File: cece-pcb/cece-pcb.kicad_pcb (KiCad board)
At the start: 2 copper layers, 57 x 80.5 mm, 52 parts, among them J1 SERIAL, J2 HTU21D, J3 Li-Ion Battery, J4 VAC, K1 SANYOU_SRD_Form_C, Q1 Q_NPN, Q2 Q_NPN, SW1 RES, U1 ESP-12F, U2 MCP73811T-420I-OT, U3 TLV75533PDBV

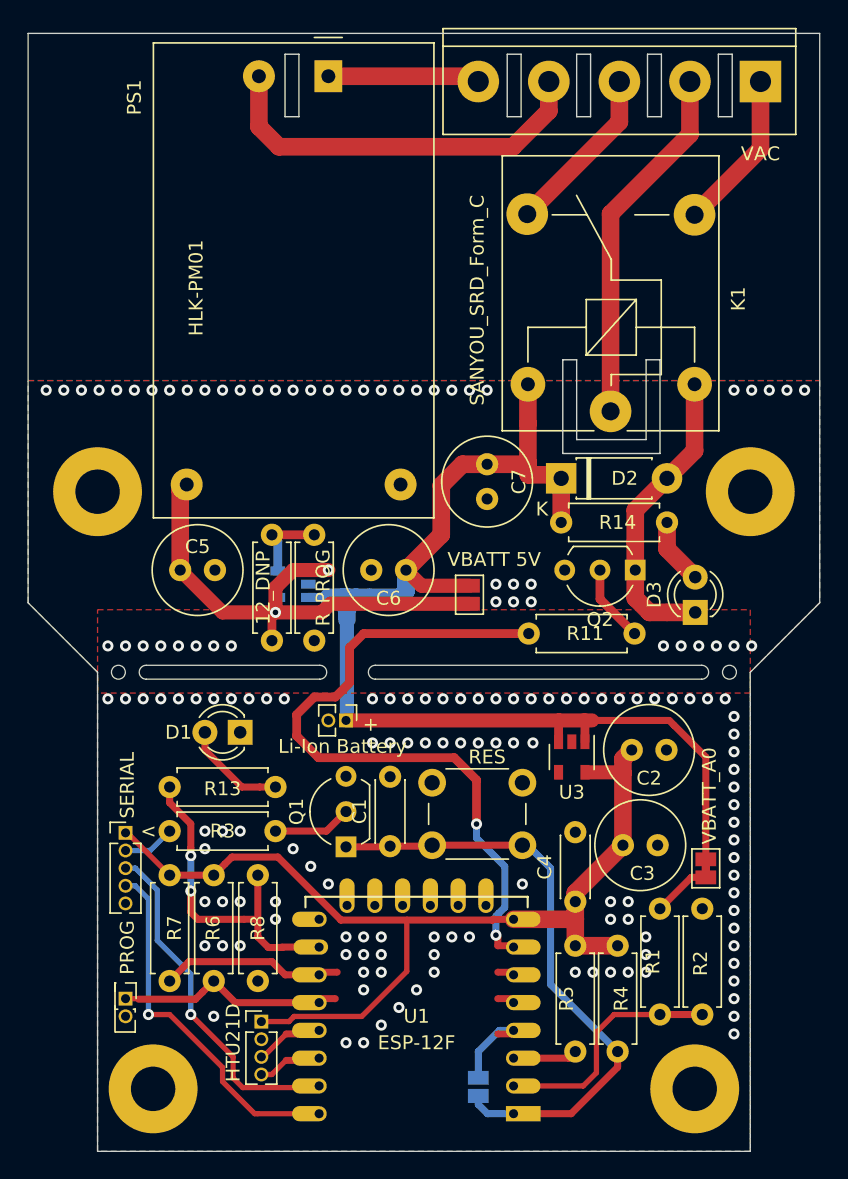
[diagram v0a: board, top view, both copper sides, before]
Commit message: Fix wrong footprint for the pin headers
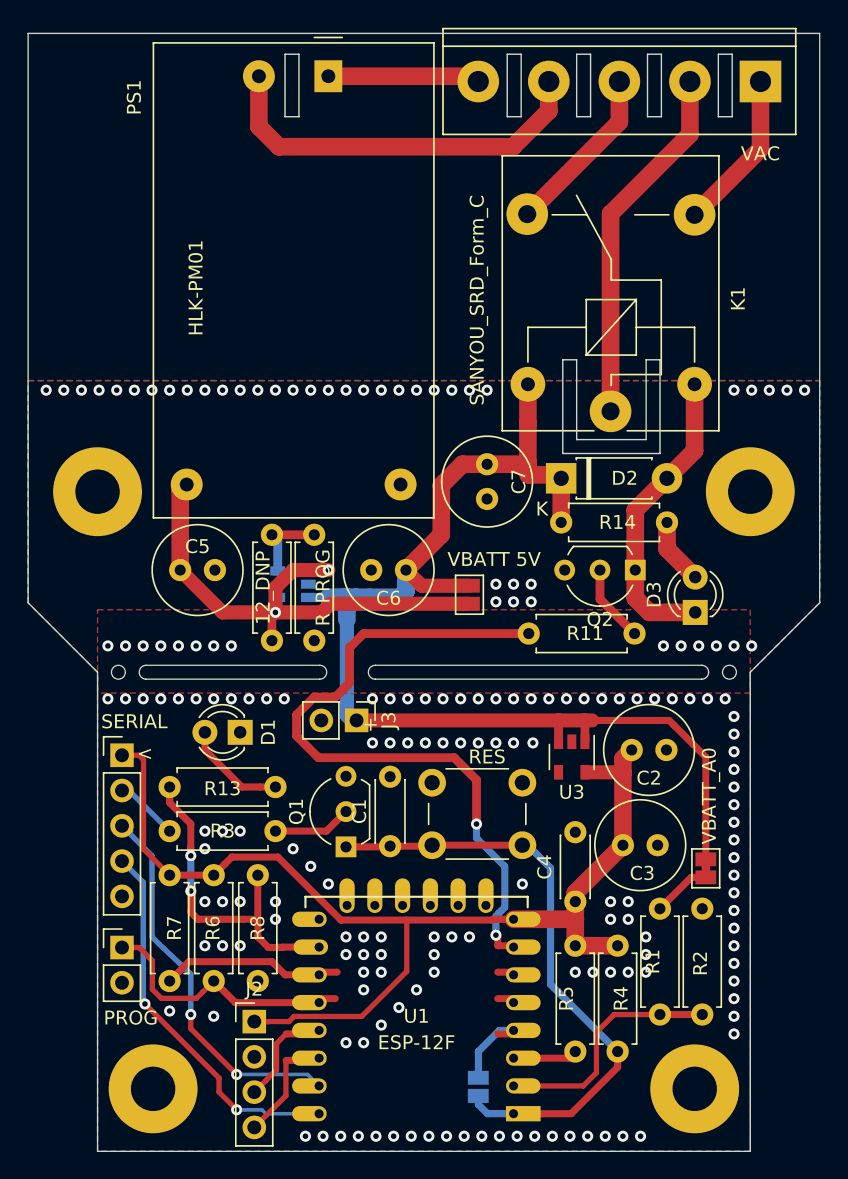
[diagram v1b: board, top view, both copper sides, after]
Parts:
- J1: footprint Connector_PinHeader_1.27mm:PinHeader_1x05_P1.27mm_Vertical -> Connector_PinHeader_2.54mm:PinHeader_1x05_P2.54mm_Vertical
- J2: footprint Connector_PinHeader_1.27mm:PinHeader_1x04_P1.27mm_Vertical -> Connector_PinHeader_2.54mm:PinHeader_1x04_P2.54mm_Vertical
- J3: footprint Connector_PinHeader_1.27mm:PinHeader_1x02_P1.27mm_Vertical -> Connector_PinHeader_2.54mm:PinHeader_1x02_P2.54mm_Vertical
- JP11: footprint Connector_PinHeader_1.27mm:PinHeader_2x01_P1.27mm_Vertical -> Connector_PinHeader_2.54mm:PinHeader_1x02_P2.54mm_Vertical
- moved J1 5.59 mm to (119.8, 86.0)
- moved JP11 3.69 mm to (119.8, 99.8), turned to 0 degrees
- moved J3 0.76 mm to (136.7, 83.5)
- moved J2 0.51 mm to (129.3, 105.2)
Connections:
- NT1 pad 1: (no net) -> /ESP-12_common/D0
- NT2 pad 1: (no net) -> /ESP-12_common/D5|SCK
- NT3 pad 1: (no net) -> /ESP-12_common/D6|MISO
- NT8 pad 2: (no net) -> /ESP-12_common/D3
- NT9 pad 2: (no net) -> /ESP-12_common/D4
- U1 pad 17: (no net) -> Net-(U1-Pad17)
- U1 pad 18: (no net) -> Net-(U1-Pad18)
- U1 pad 19: (no net) -> Net-(U1-Pad19)
- U1 pad 20: (no net) -> Net-(U1-Pad20)
- U1 pad 21: (no net) -> Net-(U1-Pad21)
- U1 pad 22: (no net) -> Net-(U1-Pad22)
- U3 pad 4: (no net) -> Net-(U3-Pad4)
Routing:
- net +3V3: track 73.3 -> 80.6 mm
- net /HTU_SCL: track 2.19 -> 5.77 mm
- net /RX: track 26.6 -> 29.8 mm, vias 1 -> 2
- net /ESP-12_common/GPIO0: track 16.7 -> 19.6 mm
- net /HTU_SDA: track 2.47 -> 5.14 mm
- net +BATT: track 89.4 -> 90.8 mm
- net /TX: track 26.2 -> 27.5 mm, vias 1 -> 2
- net /DTR: track 3.75 -> 4.64 mm
- net GND: track 0.00 -> 0.13 mm, vias 159 -> 180

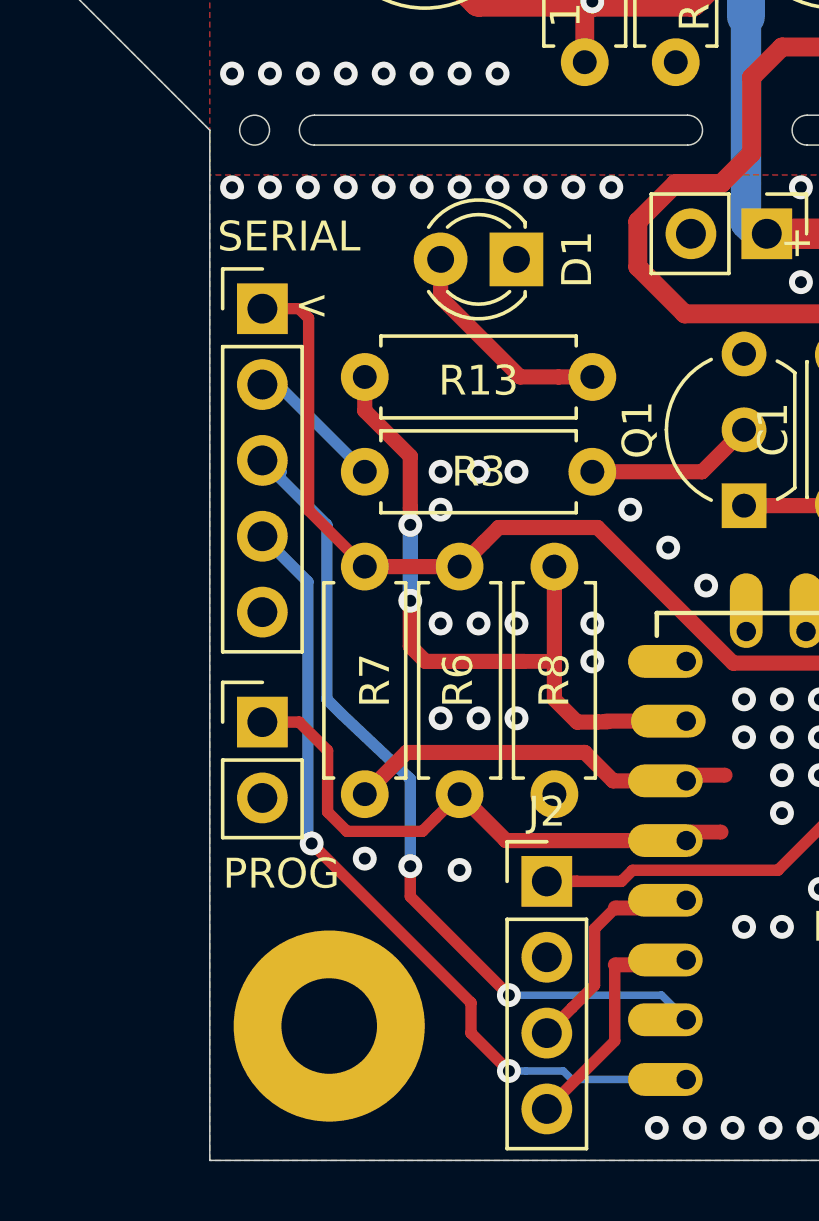
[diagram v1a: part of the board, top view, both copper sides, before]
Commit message: Create gerbers with the fixed pin header size
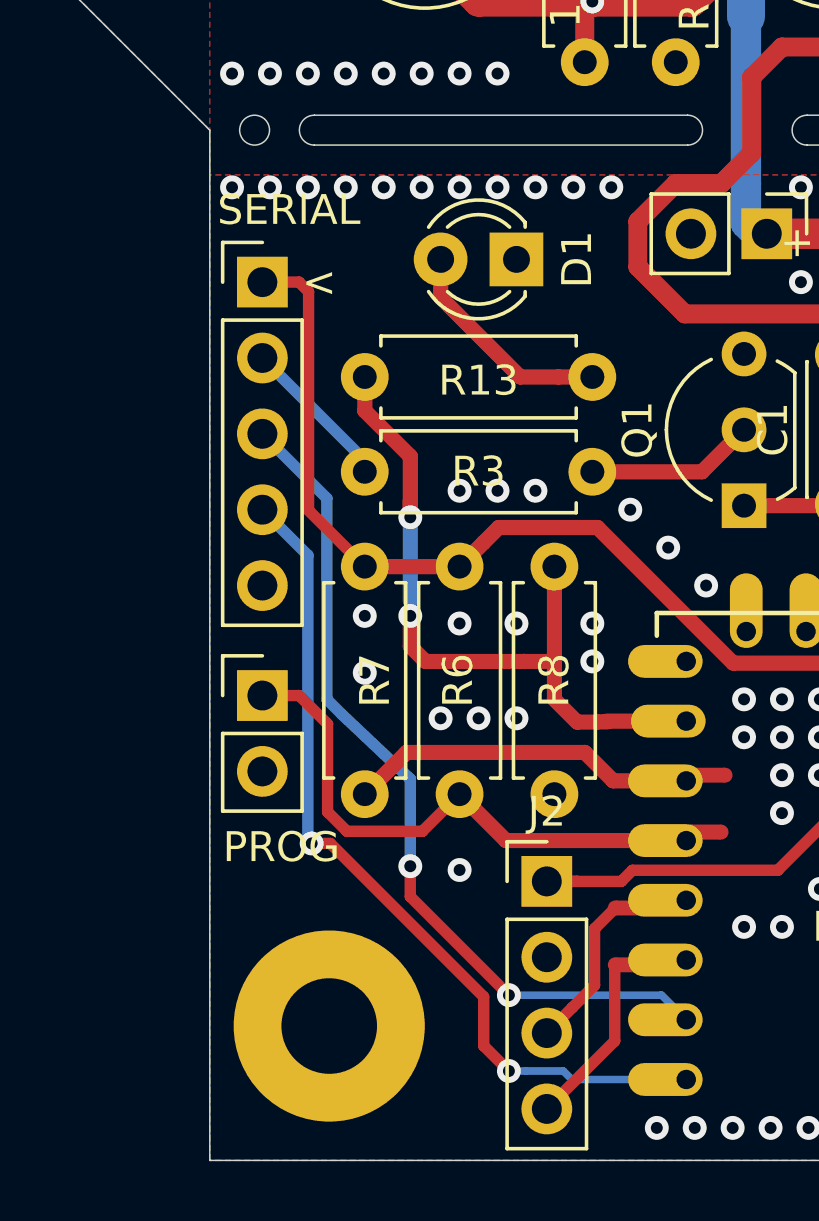
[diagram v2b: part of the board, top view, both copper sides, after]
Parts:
- added REF**: a_black_cat, pol:a_black_cat, B.Cu at (126.4, 61.0)
- moved J1 0.89 mm to (119.8, 85.1)
- moved JP11 0.89 mm to (119.8, 98.9)
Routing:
- net /TX: track 27.5 -> 28.6 mm
- net +3V3: track 80.6 -> 81.5 mm
- net /ESP-12_common/GPIO0: track 19.6 -> 20.5 mm
- net /DTR: track 4.64 -> 5.23 mm
- net /ESP-12_common/D8: track 13.7 -> 13.2 mm
- net GND: vias 180 -> 179

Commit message: Update PCB
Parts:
- removed J1: SERIAL, Connector_PinHeader_2.54mm:PinHeader_1x05_P2.54mm_Vertical
- removed J2: HTU21D, Connector_PinHeader_2.54mm:PinHeader_1x04_P2.54mm_Vertical
- removed JP1: Deep_Sleep, Jumper:SolderJumper-2_P1.3mm_Open_Pad1.0x1.5mm
- removed JP11: PROG, Connector_PinHeader_2.54mm:PinHeader_1x02_P2.54mm_Vertical
- removed NT1: D0/GPIO16, NetTie:NetTie-2_SMD_Pad0.5mm
- removed NT2: D5/GPIO14, NetTie:NetTie-2_SMD_Pad0.5mm
- removed NT3: D6/GPIO12, NetTie:NetTie-2_SMD_Pad0.5mm
- removed NT4: D7/GPIO13, NetTie:NetTie-2_SMD_Pad0.5mm
- removed NT5: D8/GPIO15, NetTie:NetTie-2_SMD_Pad0.5mm
- removed NT6: D1/GPIO5, NetTie:NetTie-2_SMD_Pad0.5mm
- removed NT7: D2/GPIO4, NetTie:NetTie-2_SMD_Pad0.5mm
- removed NT8: D3/GPIO0, NetTie:NetTie-2_SMD_Pad0.5mm
- removed NT9: D4/GPIO2, NetTie:NetTie-2_SMD_Pad0.5mm
- removed Q1: Q_NPN, Package_TO_SOT_THT:TO-92L_Inline_Wide
- removed R13: 1k, Resistor_THT:R_Axial_DIN0207_L6.3mm_D2.5mm_P7.62mm_Horizontal
- removed R3: 10k, Resistor_THT:R_Axial_DIN0207_L6.3mm_D2.5mm_P7.62mm_Horizontal
- removed R9: 12_DNP, Resistor_THT:R_Axial_DIN0207_L6.3mm_D2.5mm_P7.62mm_Horizontal
- removed REF**: a_black_cat, pol:a_black_cat
- added J102: HTU21D, Connector_PinHeader_2.54mm:PinHeader_1x04_P2.54mm_Vertical, F.Cu at (129.3, 102.4)
- added J103: SERIAL, Connector_PinHeader_2.54mm:PinHeader_1x04_P2.54mm_Vertical, F.Cu at (119.8, 85.6)
- added JP201: PROG, Connector_PinHeader_2.54mm:PinHeader_1x02_P2.54mm_Vertical, F.Cu at (119.8, 98.6)
- added JP202: Deep_Sleep, Jumper:SolderJumper-2_P1.3mm_Open_Pad1.0x1.5mm, B.Cu at (145.4, 109.9)
- added R102: 12_DNP, Resistor_THT:R_Axial_DIN0207_L6.3mm_D2.5mm_P7.62mm_Horizontal, F.Cu at (130.6, 77.7)
- added R104: 100, Resistor_THT:R_Axial_DIN0207_L6.3mm_D2.5mm_P7.62mm_Horizontal, F.Cu at (135.9, 94.0)
- R101: renamed from R14; value 1k -> 220
- R103: renamed from R11; value R_US -> 1k
- moved R204 4.67 mm to (126.6, 99.1)
- moved R203 4.31 mm to (123.4, 99.1)
- moved R206 3.19 mm to (129.8, 99.1)
- moved D103 1.63 mm to (127.0, 85.3), turned to 0 degrees
- moved U201 0.60 mm to (148.0, 112.4)
- renumbered C7 to C101, C5 to C102, C6 to C103, C1 to C201, C2 to C202, C3 to C203, C4 to C204, D2 to D101, D3 to D102, D1 to D103, H1 to H101, H2 to H102, H3 to H103, H4 to H104, J4 to J101, J3 to J104, JP2 to JP101, JP3 to JP102, K1 to K101, PS1 to PS101, Q2 to Q101, R10 to R105, R4 to R201, R5 to R202, R6 to R203, R7 to R204, R1 to R205, R8 to R206, R2 to R207, SW1 to SW201, U3 to U101, U2 to U102, U1 to U201
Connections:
- R203 pad 1: /ESP-12_common/GPIO0 -> /ESP-12_common/D3
- R204 pad 1: /ESP-12_common/GPIO2 -> /ESP-12_common/D4
- R206 pad 2: /ESP-12_common/GPIO15 -> /ESP-12_common/D8
- U201 pad 10: /ESP-12_common/GPIO15 -> /ESP-12_common/D8
- U201 pad 11: /ESP-12_common/GPIO2 -> /ESP-12_common/D4
- U201 pad 12: /ESP-12_common/GPIO0 -> /ESP-12_common/D3
- U201 pad 13: /ESP-12_common/GPIO4 -> /HTU_SDA
- U201 pad 14: /ESP-12_common/GPIO5 -> /HTU_SCL
- U201 pad 4: /ESP-12_common/GPIO16 -> /ESP-12_common/D0
- U201 pad 5: /ESP-12_common/GPIO14 -> /ESP-12_common/D5|SCK
- U201 pad 6: /ESP-12_common/GPIO12 -> /ESP-12_common/D6|MISO
- U201 pad 7: /ESP-12_common/GPIO13 -> /RLY
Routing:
- net /ESP-12_common/GPIO0: track 20.5 -> 0.00 mm
- net /ESP-12_common/D3: track 0.00 -> 19.7 mm
- net /ESP-12_common/GPIO2: track 13.4 -> 0.00 mm
- net /ESP-12_common/D4: track 0.00 -> 11.5 mm
- net /ESP-12_common/GPIO15: track 10.9 -> 0.00 mm
- net Net-(Q1-Pad2): track 5.66 -> 0.00 mm
- net /DTR: track 5.23 -> 0.00 mm
- net /ESP-12_common/GPIO16: track 5.06 -> 0.00 mm
- net /ESP-12_common/D0: track 0.00 -> 4.81 mm
- net /RX: track 30.0 -> 33.9 mm
- net /ESP-12_common/D8: track 13.2 -> 16.8 mm, vias 2 -> 0
- net /ESP-12_common/RST: track 44.4 -> 47.0 mm, vias 0 -> 2
- net /TX: track 28.6 -> 30.9 mm
- net /ESP-12_common/ADC: track 17.4 -> 16.5 mm
- net +3V3: track 81.5 -> 80.9 mm
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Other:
- board text added: "3V3"
- board text added: "<A0"
- board text added: "<D1"
- board text added: "<D2"
- board text added: "<D3"
- board text added: "<D4"
- board text added: "<D8"
- board text added: "<RX"
- board text added: "<TX"
- board text added: "CECE r1.0"
- board text added: "D0>"
- board text added: "D5>"
- board text added: "D6>"
- board text added: "D7>"
- board text added: "GND"
- board text added: "RX"
- board text added: "TX"

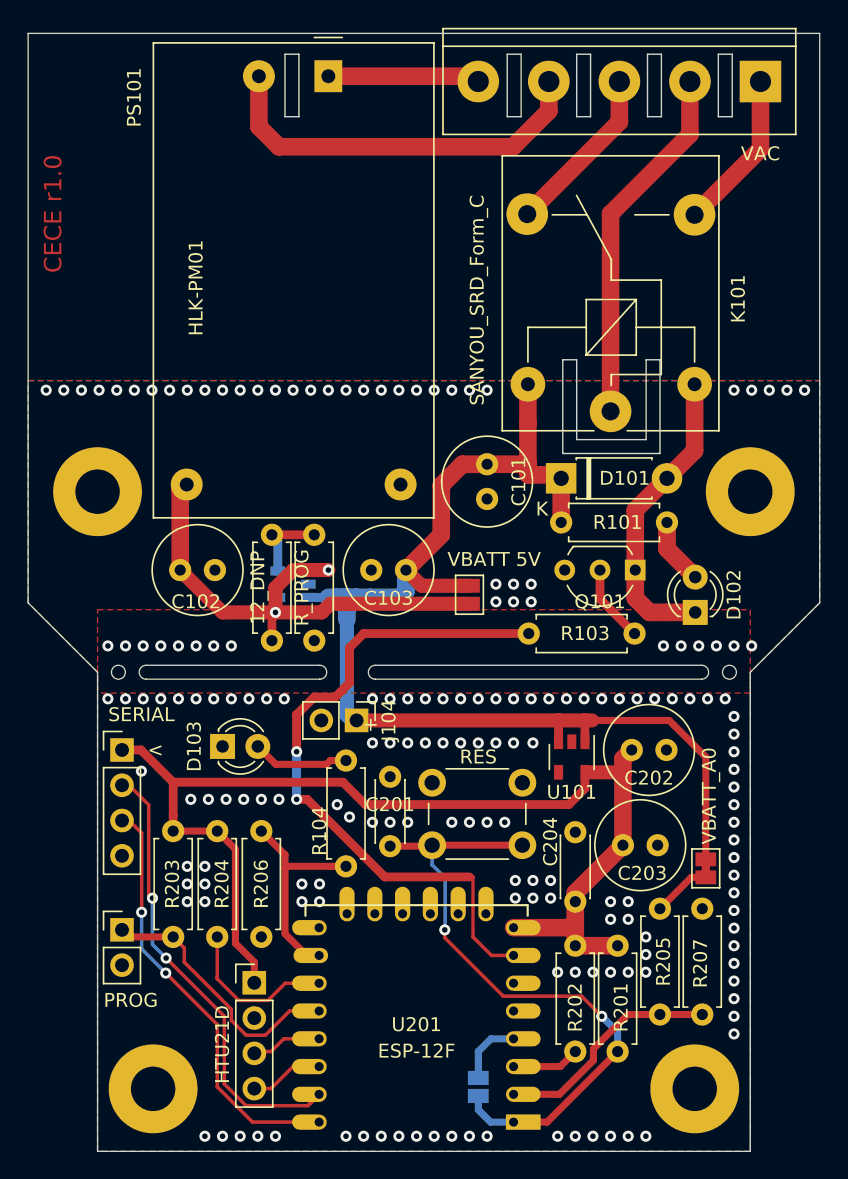
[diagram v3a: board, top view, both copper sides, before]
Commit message: Increase thermal relief size for easier hand soldering
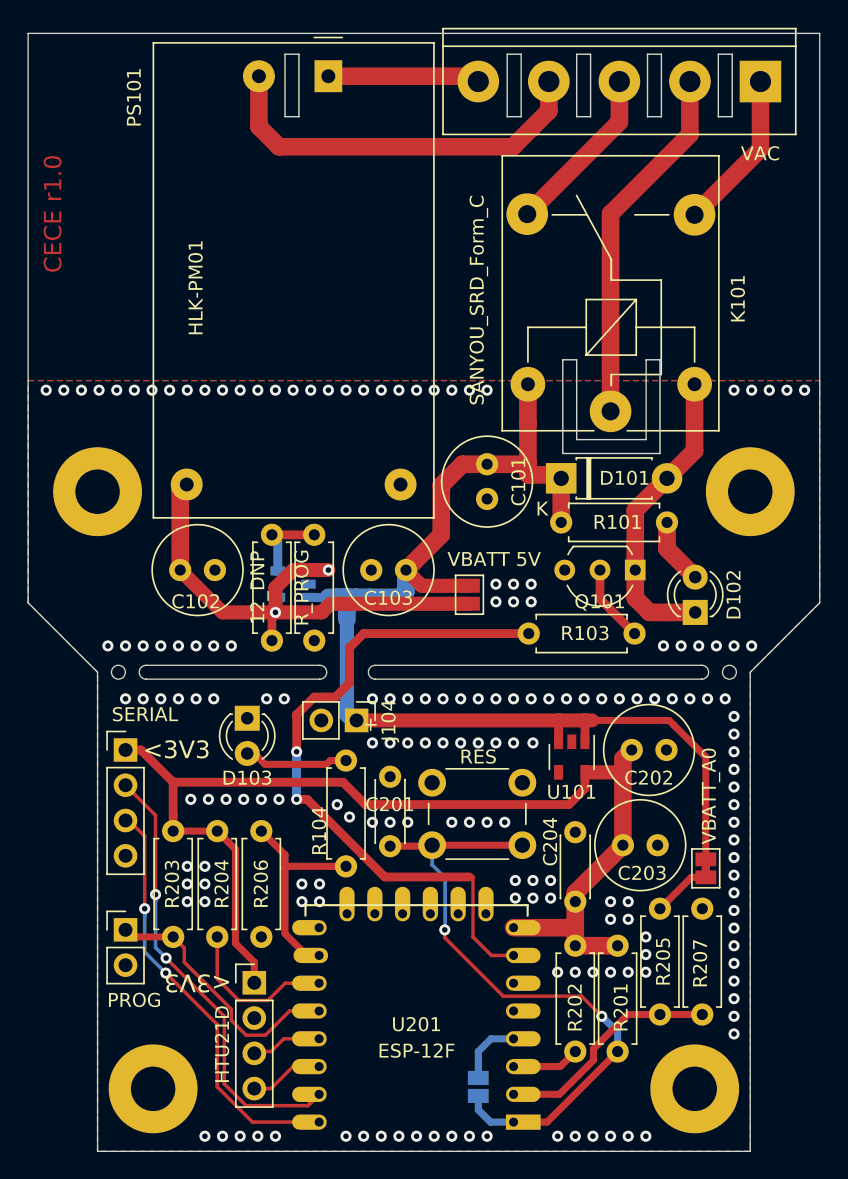
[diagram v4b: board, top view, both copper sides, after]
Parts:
- moved D103 2.70 mm to (128.8, 83.3), turned to 270 degrees
- moved J103 0.25 mm to (120.0, 85.6)
- moved JP201 0.25 mm to (120.0, 98.6)
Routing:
- net Net-(D103-Pad2): track 7.00 -> 7.76 mm
- net /TX: track 30.9 -> 31.4 mm
- net GND: vias 176 -> 172
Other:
- board text added: "<3V3"
- board text removed: "<"
